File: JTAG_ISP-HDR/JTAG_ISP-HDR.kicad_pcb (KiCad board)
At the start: 2 copper layers, 23.1 x 46.1 mm, 10 parts, among them J1 Conn_01x08, J2 Conn_01x08

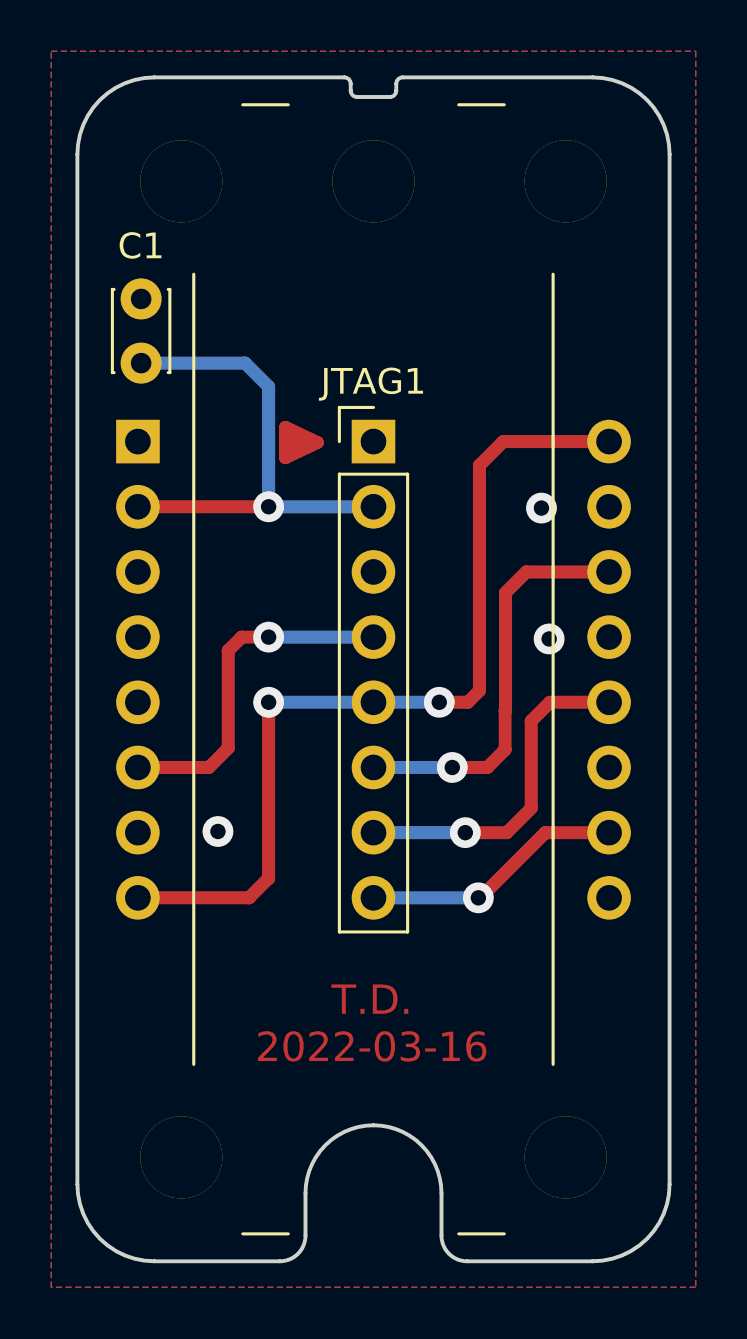
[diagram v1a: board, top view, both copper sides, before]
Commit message: # [PCB] + Ajout de GND et de VCC dans le projet HDR sur les broches non utilisés de J1 & J2.     + Ajout des nouveaux vias. * Projet HDR routé à nouveau. * Utilisation de trous de montage avec pads. * Flèche d'indication de la broche #1 pour le PICKit4 dans le projet HDR est déplacée pour s'alligner avec celle sur le PICKit4. * Modification du texte (initiales et date du jour) sur le PCB du projet HDR.
# [SCHÉMA]
+ Ajout de GND et de VCC dans le projet HDR sur les broches non utilisées de J1 & J2.
    + Ajout des nouveaux noms de broches sur J1 & J2.
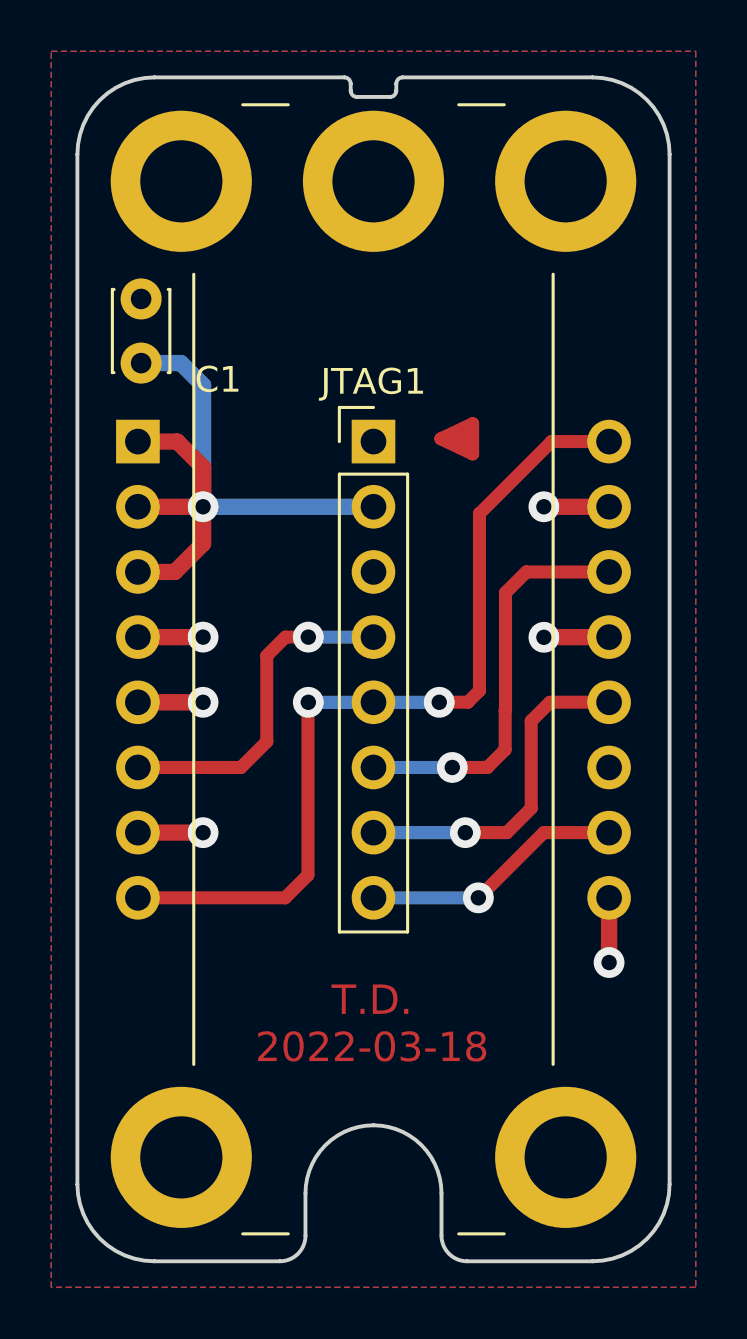
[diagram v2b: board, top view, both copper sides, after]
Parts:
- removed the REF** at (156.4, 65.4)
- removed the REF** at (148.9, 65.4)
- removed the REF** at (163.8, 103.4)
- removed the REF** at (148.9, 103.4)
- removed the REF** at (163.8, 65.4)
- added REF**: MountingHole_3.2mm_M3_ISO14580_Pad, MountingHole:MountingHole_3.2mm_M3_ISO14580_Pad, F.Cu at (156.4, 65.4)
- added REF**: MountingHole_3.2mm_M3_ISO14580_Pad, MountingHole:MountingHole_3.2mm_M3_ISO14580_Pad, F.Cu at (163.8, 103.4)
- added REF**: MountingHole_3.2mm_M3_ISO14580_Pad, MountingHole:MountingHole_3.2mm_M3_ISO14580_Pad, F.Cu at (148.9, 103.4)
- added REF**: MountingHole_3.2mm_M3_ISO14580_Pad, MountingHole:MountingHole_3.2mm_M3_ISO14580_Pad, F.Cu at (148.9, 65.4)
- added REF**: MountingHole_3.2mm_M3_ISO14580_Pad, MountingHole:MountingHole_3.2mm_M3_ISO14580_Pad, F.Cu at (163.8, 65.4)
- moved REF** 7.32 mm to (160.2, 75.0), turned to 0 degrees
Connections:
- J1 pad 1: unconnected-(J1-Pad1) -> +5V
- J1 pad 3: unconnected-(J1-Pad3) -> +5V
- J1 pad 5: unconnected-(J1-Pad5) -> GND
- J1 pad 7: unconnected-(J1-Pad7) -> GND
- J2 pad 2: unconnected-(J2-Pad2) -> GND
- J2 pad 4: unconnected-(J2-Pad4) -> GND
- J2 pad 6: unconnected-(J2-Pad6) -> GND
- J2 pad 8: unconnected-(J2-Pad8) -> GND
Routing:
- net GND: track 0.00 -> 15.2 mm, vias 3 -> 6
- net +5V: track 19.2 -> 25.6 mm
- net Net-(J1-Pad8): track 34.9 -> 33.7 mm
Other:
- board text added: "T.D. 2022-03-18"
- board text removed: "T.D. 2022-03-16"

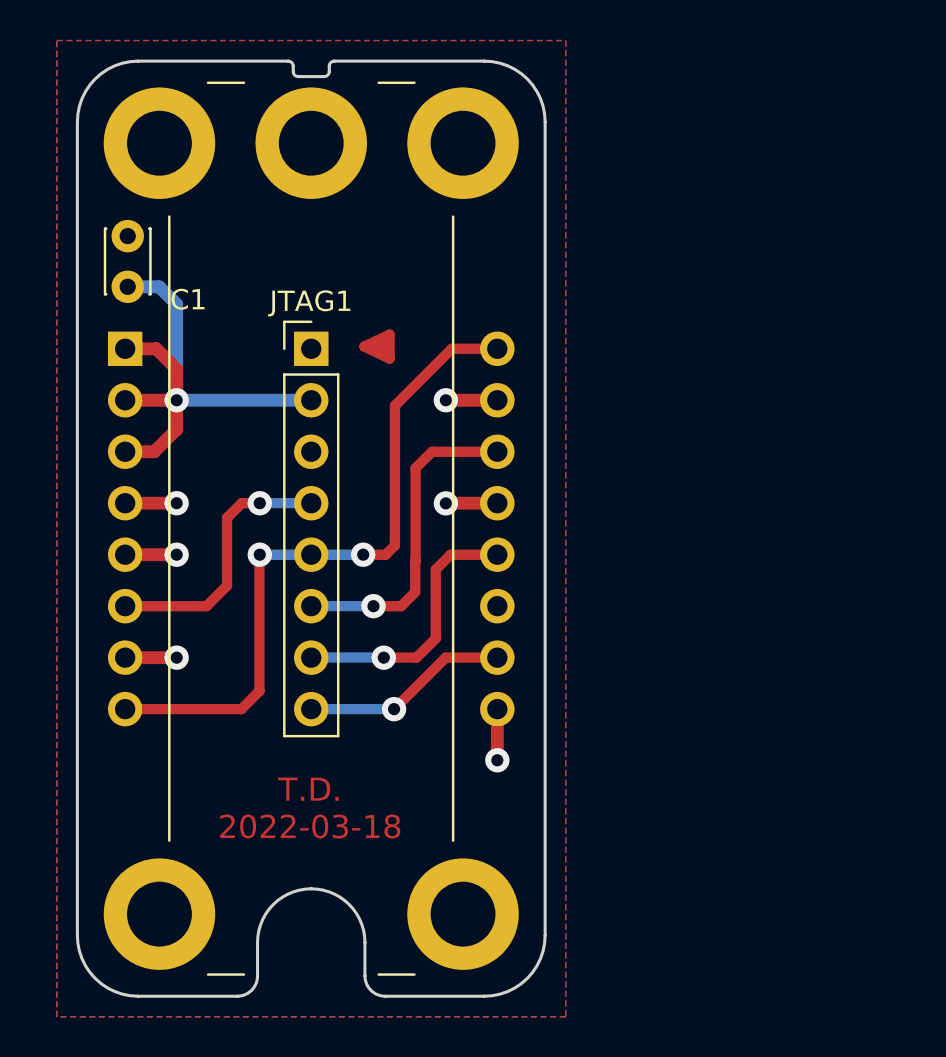
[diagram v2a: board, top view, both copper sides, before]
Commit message: # Version compacte en cours... ## Les headers passent à travers d'un PCB et dépassent moins que la version précédente.
# [PCB]
+ Ajout d'un trou pour l'ISP dans le PCB du projet HDR.
+ Ajout d'un trou pour le PICkit dans le PCB du projet ISP.
* Déplacement du circuit de DEL dans le projet HDR.
* Projet ISP routé à nouveau.
* Mise à jour de la cartouche pour les 2 projets.
    * Date actuelle;
    * Version actuelle;

# [SCHÉMA]
+ Ajout d'encadrés pointillés dan les 2 projets pour séparer les parties du schémas.
* Déplacement du circuit de DEL dans le projet HDR.
* Réduction de la valeur de la résistance pour le circuit de DEL.
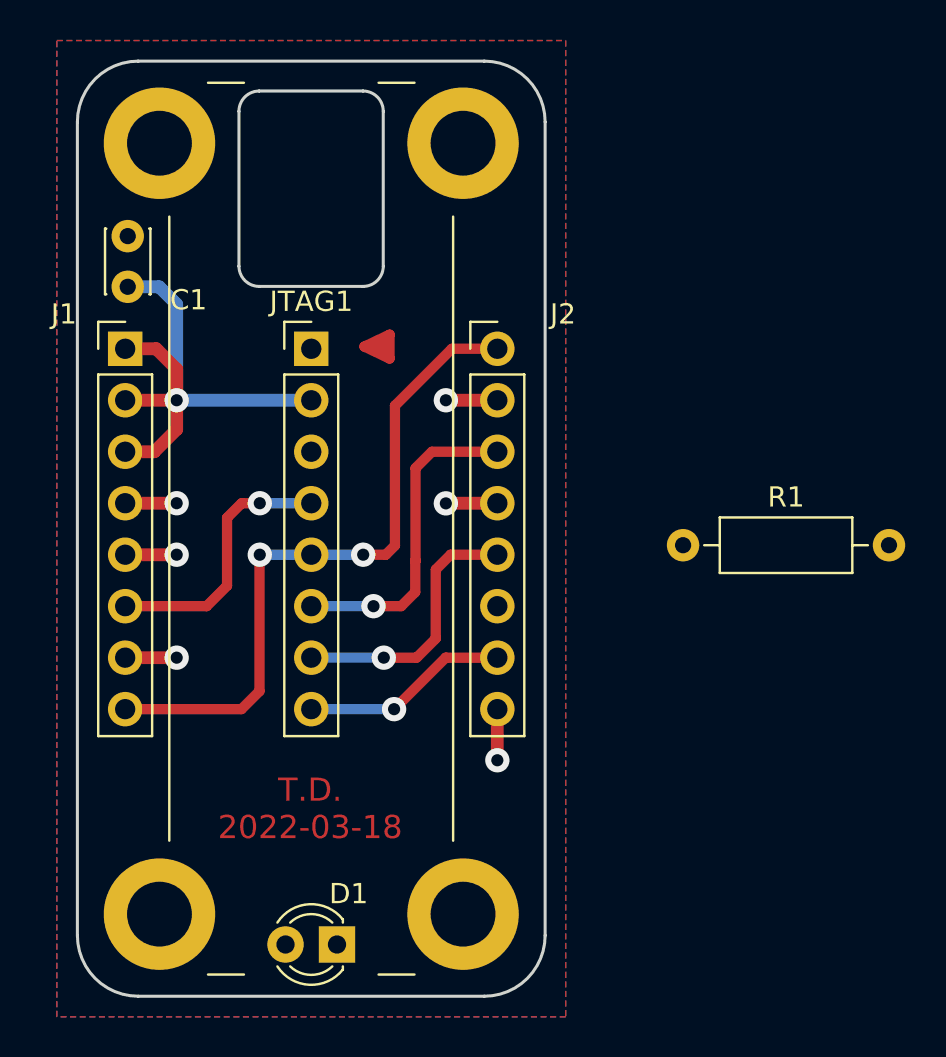
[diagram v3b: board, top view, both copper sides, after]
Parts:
- removed the REF** at (156.4, 65.4)
- added D1: LED, LED_THT:LED_D3.0mm, F.Cu at (157.6, 104.9)
- added R1: 100, Resistor_THT:R_Axial_DIN0207_L6.3mm_D2.5mm_P10.16mm_Horizontal, F.Cu at (174.7, 85.2)
- J1, J2: moved to F.Cu
- turned J2 to 0 degrees
- turned J1 to 0 degrees
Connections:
- net Net-(J1-Pad6) renamed TDO
- net Net-(J1-Pad8) renamed TCK
- net Net-(J2-Pad3) renamed RESET
- net Net-(J2-Pad5) renamed TDI
- net Net-(J2-Pad7) renamed TMS
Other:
- outline, holes or cut-outs redrawn

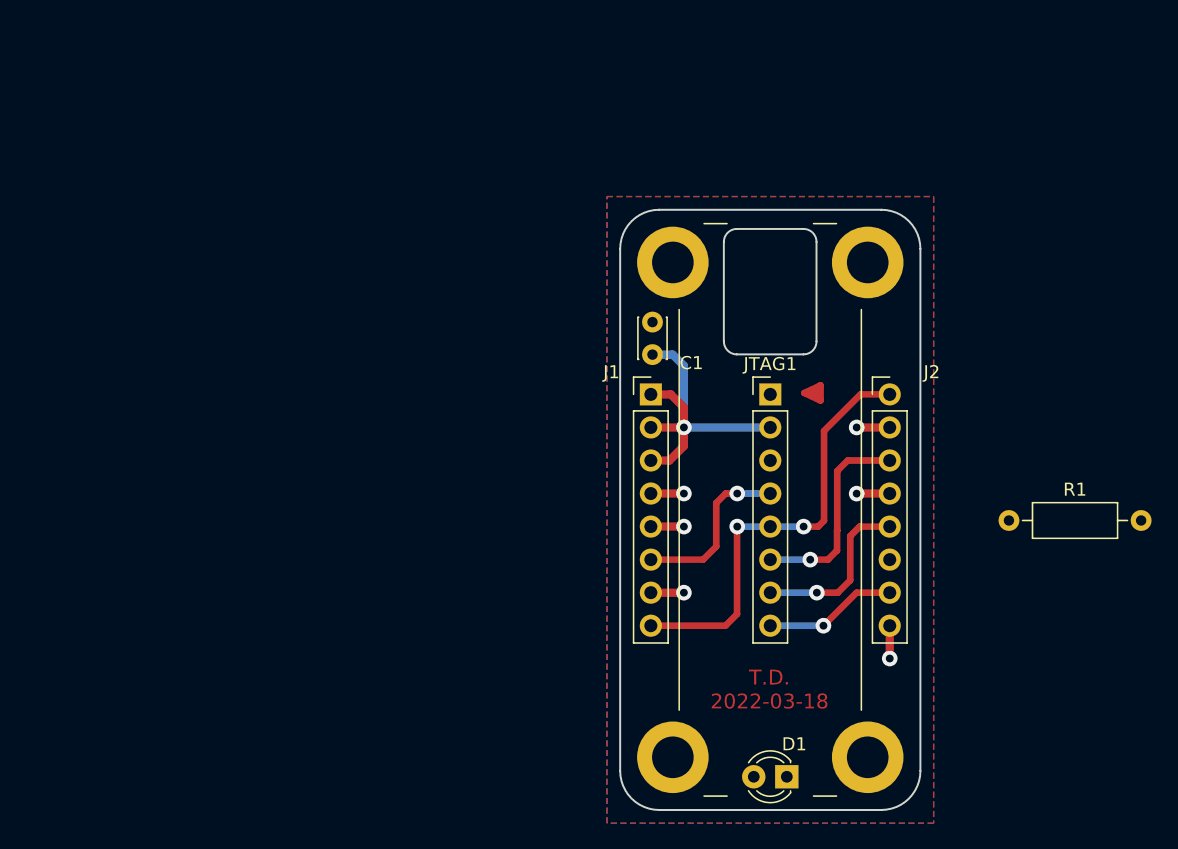
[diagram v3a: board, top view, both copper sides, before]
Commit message: # [PCB] + Ajout du dégagement de 40 mils sur la bordure du trou au centre du PCB et sur le pourtour. + Ajout de la flèche indiquand la broche #1 du header du ISP. + Double vias pour les traces d'alimentation. - Suppression du texte (date du jour) dans le bas du PCB. - Suppression de la flèche indiquand la broche #1 du header PICkit4. * Nouveau format de page A5. * PCB routé à nouveau. * Mise à jour de la cartouche.     * Date actuelle;     * Version actuelle.
# [SCHÉMA]
* Mise à jour de la cartouche.
    * Date actuelle;
    * Version actuelle.
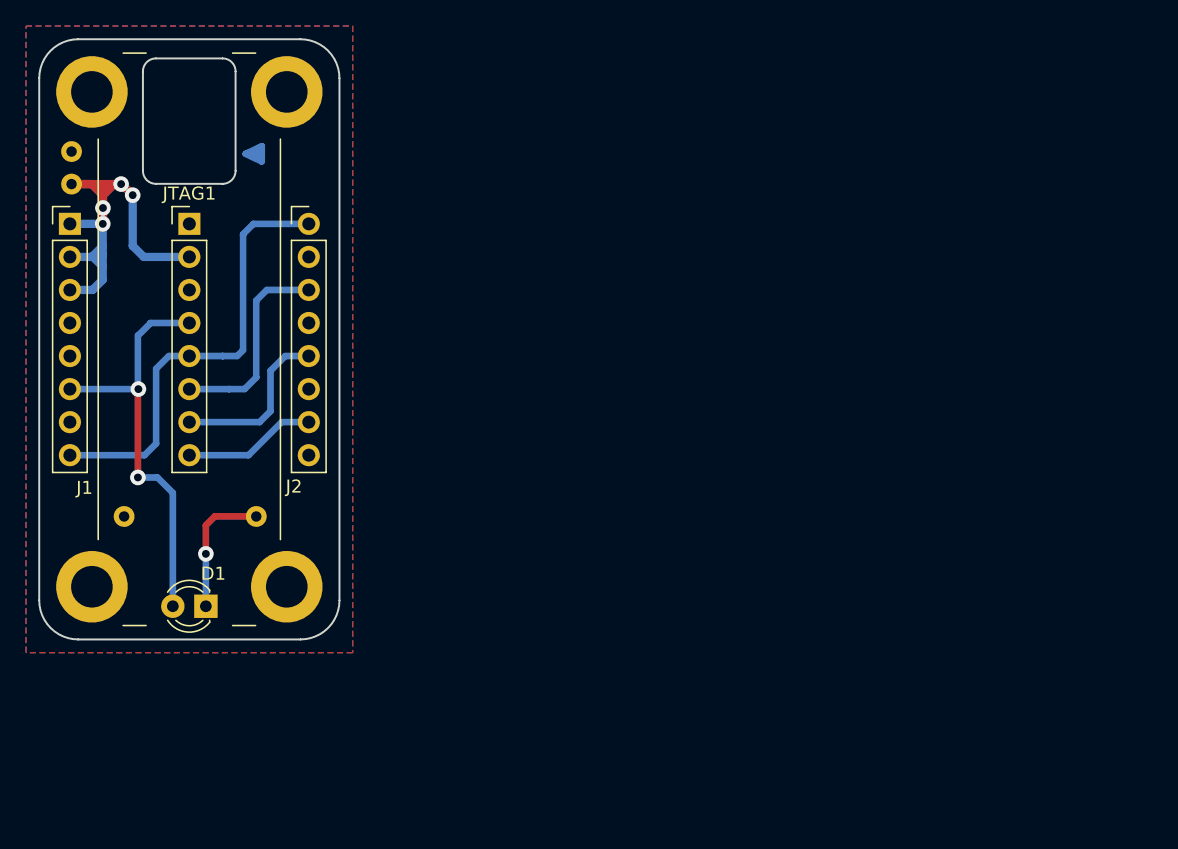
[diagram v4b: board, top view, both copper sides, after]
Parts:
- C1, R1, REF**: moved to B.Cu
- moved R1 57.9 mm to (116.9, 84.9), turned to 180 degrees
- moved JTAG1 46.5 mm to (111.7, 62.4)
- moved REF** 46.5 mm to (104.2, 90.3)
- moved REF** 46.5 mm to (104.2, 52.3)
- moved D1 46.5 mm to (113.0, 91.8)
- moved J1 46.5 mm to (102.5, 62.4)
- moved J2 46.5 mm to (120.9, 62.4)
- moved REF** 46.5 mm to (119.2, 90.3)
- moved REF** 46.5 mm to (119.2, 52.3)
- moved C1 46.5 mm to (102.7, 59.3)
- moved REF** 46.4 mm to (117.3, 57.4)
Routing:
- net TDO: track 13.2 -> 32.4 mm, vias 1 -> 2
- net GND: track 15.2 -> 0.02 mm, vias 6 -> 0
- net +5V: track 25.6 -> 37.8 mm, vias 1 -> 4
- net Net-(D1-Pad1): track 0.00 -> 10.4 mm, vias 0 -> 1
- net TCK: track 33.7 -> 34.3 mm, vias 2 -> 0
- net TDI: track 12.8 -> 13.1 mm, vias 1 -> 0
- net RESET: track 15.9 -> 15.8 mm, vias 1 -> 0
- net TMS: vias 1 -> 0
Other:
- board text removed: "T.D. 2022-03-18"

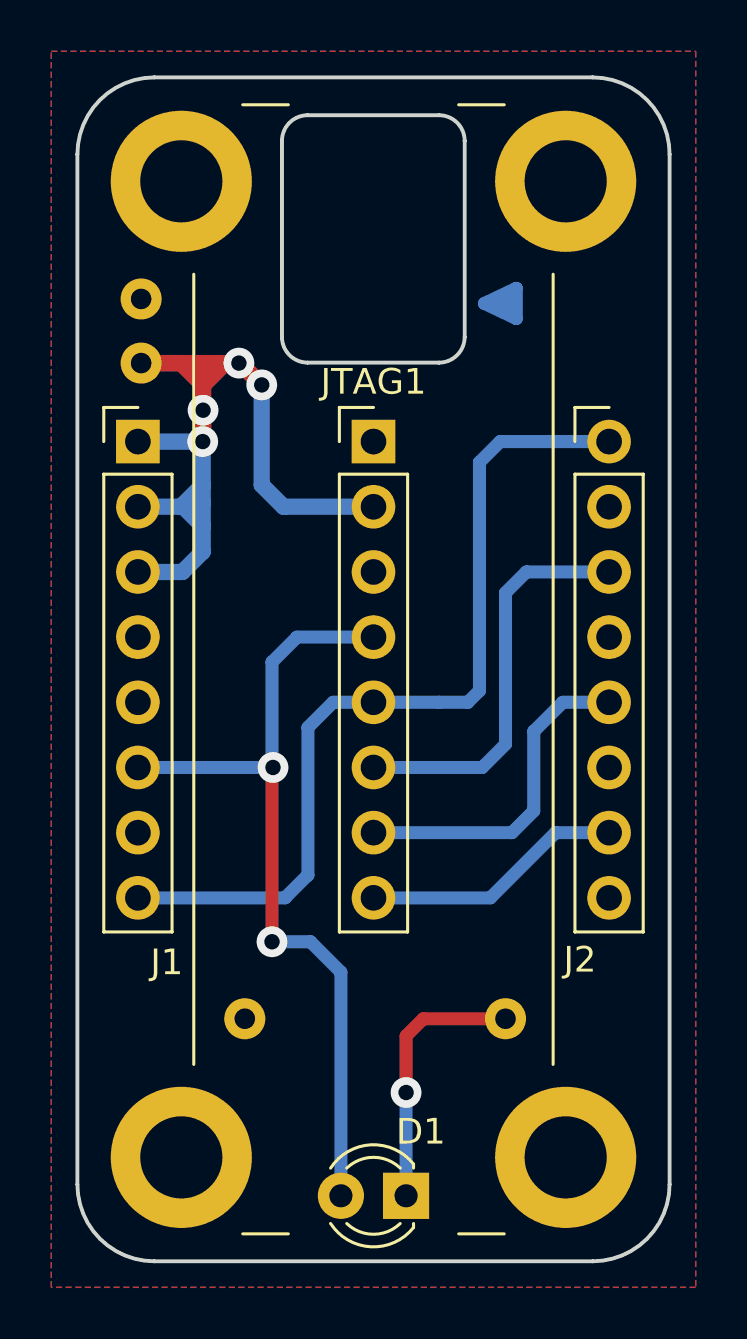
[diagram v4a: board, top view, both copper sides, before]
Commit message: # [PCB] + Ajout de vias pour le ground. + Routage du ground. - Suppression des double vias pour les traces d'alimentation. * Mise à jour de la cartouche.     * Date actuelle;     * Version actuelle.
# [SCHÉMA]
* Mise à jour de la cartouche.
    * Date actuelle;
    * Version actuelle.
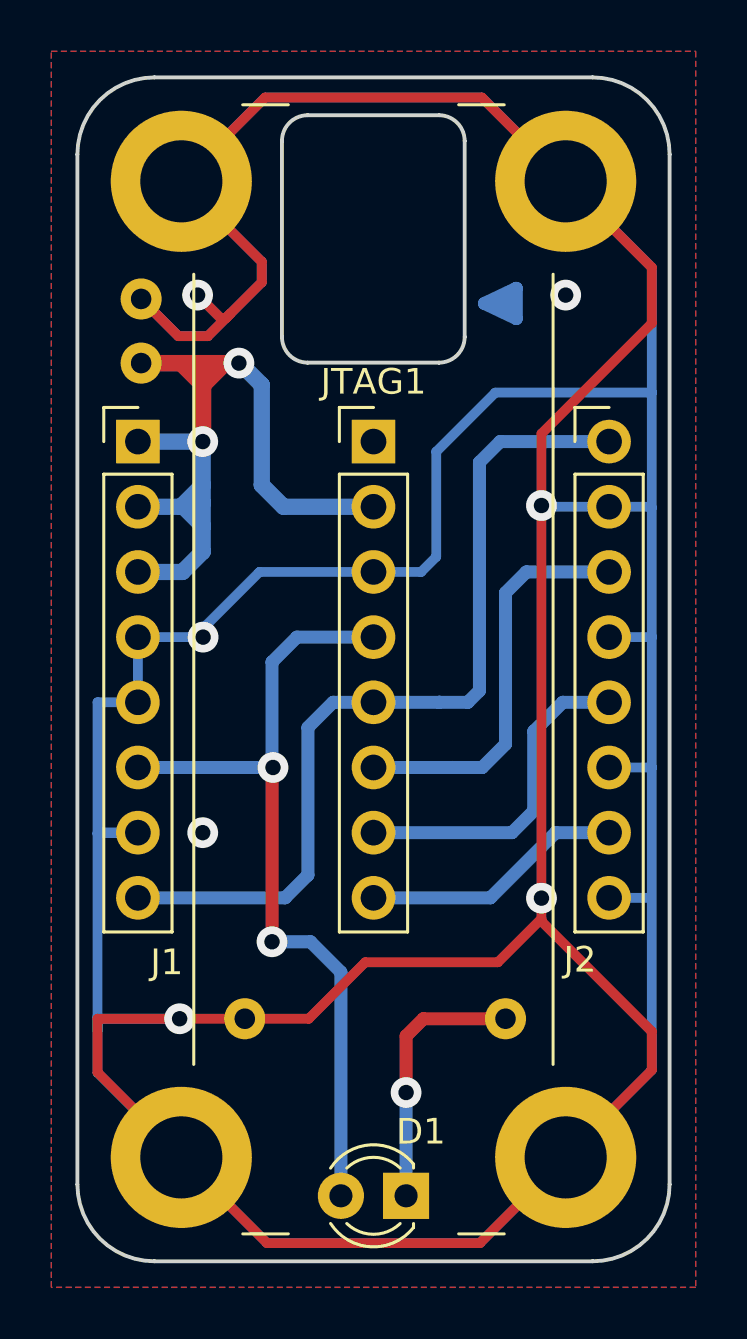
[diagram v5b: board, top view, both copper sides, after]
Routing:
- net GND: track 0.02 -> 273.3 mm, vias 0 -> 7
- net +5V: track 37.8 -> 35.3 mm, vias 4 -> 2
